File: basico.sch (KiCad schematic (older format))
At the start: 8 parts, among them P1 Power, P2 Analog, P3 Analog, P4 Digital, P5 PWM, P6 PWM, P7 Communication

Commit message: Clean up and add copper text
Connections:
- no-connect marks 63 -> 66
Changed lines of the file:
@@
 	7000 2050 7000 2150
 Wire Wire Line
-	7000 2050 7450 2050
+	7000 2050 7200 2050
 NoConn ~ 9350 1350
 Text Label 9250 1200 1    60   ~ 0
@@
 NoConn ~ 10000 4650
 NoConn ~ 10100 5650
-NoConn ~ 10300 4650
 NoConn ~ 10300 5650
 NoConn ~ 10400 5650
@@
 NoConn ~ 10400 1550
 NoConn ~ 10400 1650
-NoConn ~ 10400 1750
-NoConn ~ 10400 2750
 NoConn ~ 10400 2650
 NoConn ~ 10400 2550
@@
 Text Notes 1375 675  0    60   ~ 0
 Poncho Smart RAMPS para EDU-CIAA-NXP\n
+NoConn ~ 10400 3050
+NoConn ~ 10400 3150
+NoConn ~ 10400 1150
+NoConn ~ 10400 1250
+NoConn ~ 10200 5650
+NoConn ~ 9250 1200
+$Comp
+L basico-rescue:PWR_FLAG #FLG0101
+U 1 1 5D0FAD0D
+P 7200 2050
+F 0 "#FLG0101" H 7200 2145 30  0001 C CNN
+F 1 "PWR_FLAG" H 7200 2230 30  0000 C CNN
+F 2 "" H 7200 2050 60  0000 C CNN
+F 3 "" H 7200 2050 60  0000 C CNN
+	1    7200 2050
+	-1   0    0    1
+$EndComp
+Connection ~ 7200 2050
+Wire Wire Line
+	7200 2050 7450 2050
 $EndSCHEMATC

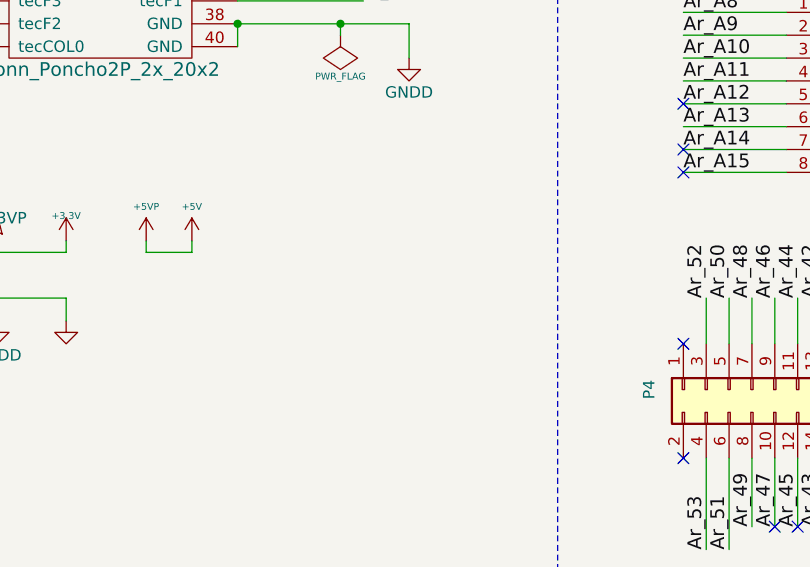
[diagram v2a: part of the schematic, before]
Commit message: Agregar led y re-ruteo
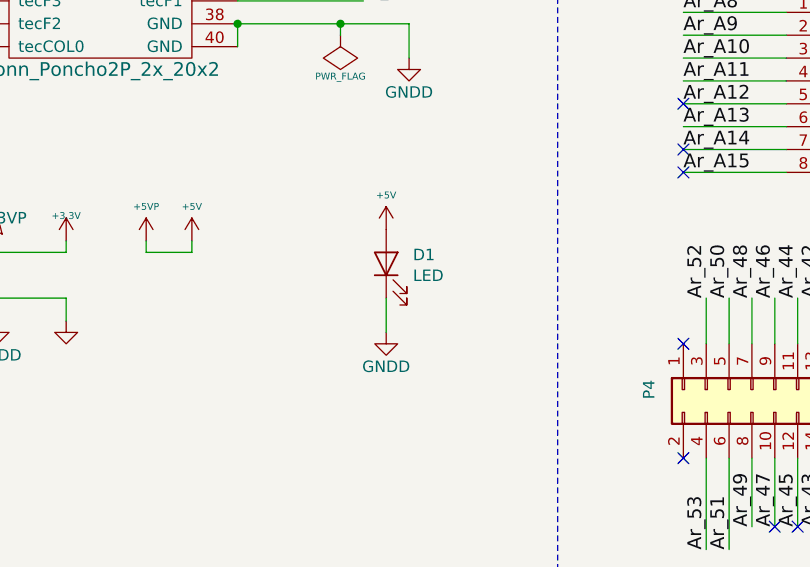
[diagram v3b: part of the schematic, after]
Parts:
- added D1: LED, LED_THT:LED_D3.0mm, symbol Device:LED
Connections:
- net +5V: now also D1.2 (A)
- net GND: now also D1.1 (K)
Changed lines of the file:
@@
 Sheet 1 1
 Title "Poncho Smart RAMPS para EDU-CIAA-NXP"
-Date "2019-06-17"
+Date "2019-06-24"
 Rev "1.0"
 Comp "Proyecto CIAA - COMPUTADORA INDUSTRIAL ABIERTA ARGENTINA"
-Comment1 "https://github.com/ciaa/Ponchos/tree/master/Basico/doc"
+Comment1 "https://github.com/dc740/smart-ramps-to-edu-ciaa"
 Comment2 "Licencia GPL v3 (Emilio Moretti - UNNOBA)"
 Comment3 "Ing. Moretti Emilio"
-Comment4 ""
+Comment4 "Revisor: Nelson Fortunatti"
 $EndDescr
 $Comp
@@
 Wire Wire Line
 	7200 2050 7450 2050
+$Comp
+L Device:LED D1
+U 1 1 5D12DF66
+P 7600 4500
+F 0 "D1" V 7639 4383 50  0000 R CNN
+F 1 "LED" V 7548 4383 50  0000 R CNN
+F 2 "LED_THT:LED_D3.0mm" H 7600 4500 50  0001 C CNN
+F 3 "~" H 7600 4500 50  0001 C CNN
+	1    7600 4500
+	0    -1   -1   0
+$EndComp
+$Comp
+L basico-rescue:+5V #PWR0103
+U 1 1 5D14A06A
+P 7600 4350
+F 0 "#PWR0103" H 7600 4440 20  0001 C CNN
+F 1 "+5V" H 7600 4500 30  0000 C CNN
+F 2 "" H 7600 4350 60  0000 C CNN
+F 3 "" H 7600 4350 60  0000 C CNN
+	1    7600 4350
+	1    0    0    -1
+$EndComp
+$Comp
+L basico-rescue:GNDD #PWR0104
+U 1 1 5D16F0C7
+P 7600 4800
+F 0 "#PWR0104" H 7600 4550 50  0001 C CNN
+F 1 "GNDD" H 7600 4650 50  0000 C CNN
+F 2 "" H 7600 4800 50  0000 C CNN
+F 3 "" H 7600 4800 50  0000 C CNN
+	1    7600 4800
+	1    0    0    -1
+$EndComp
+Wire Wire Line
+	7600 4650 7600 4800
 $EndSCHEMATC

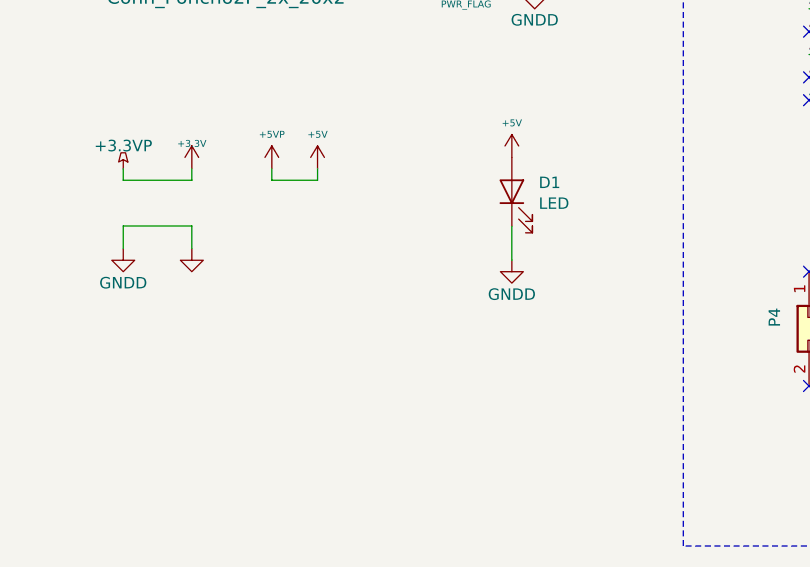
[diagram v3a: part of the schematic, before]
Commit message: Connect analog ground
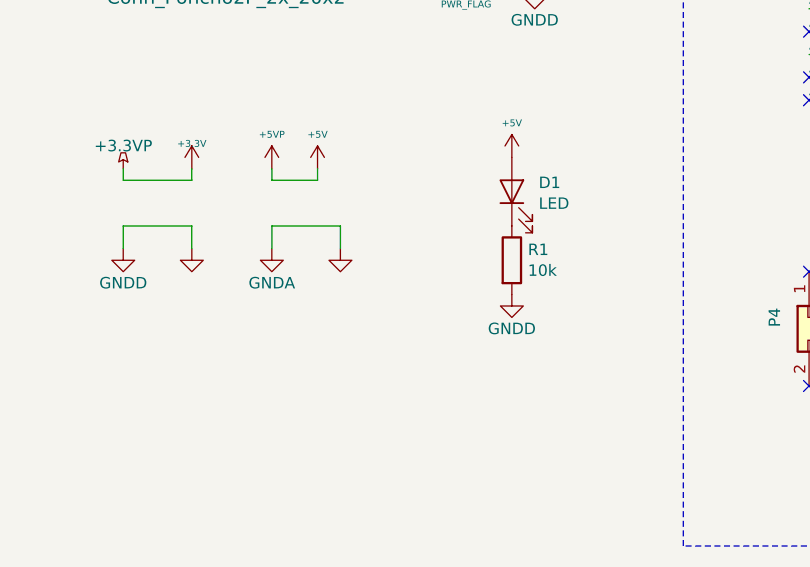
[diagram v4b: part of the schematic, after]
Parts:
- added R1: 10k, Resistor_THT:R_Axial_DIN0204_L3.6mm_D1.6mm_P5.08mm_Horizontal, symbol Device:R
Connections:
- net GNDA is gone; now on net GND: XA101.10 (GNDA), XA101.12 (GNDA), XA101.14 (GNDA), XA101.16 (GNDA), XA101.18 (GNDA), XA101.7 (GNDA), XA101.8 (GNDA)
- net GND: now also R1.2; no longer D1.1 (K)
- new net: D1.1 (K), R1.1
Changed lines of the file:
@@
 L basico-rescue:GNDD #PWR0104
 U 1 1 5D16F0C7
+P 7600 4950
+F 0 "#PWR0104" H 7600 4700 50  0001 C CNN
+F 1 "GNDD" H 7600 4800 50  0000 C CNN
+F 2 "" H 7600 4950 50  0000 C CNN
+F 3 "" H 7600 4950 50  0000 C CNN
+	1    7600 4950
+	1    0    0    -1
+$EndComp
+$Comp
+L Device:R R1
+U 1 1 5D13D3F8
 P 7600 4800
-F 0 "#PWR0104" H 7600 4550 50  0001 C CNN
-F 1 "GNDD" H 7600 4650 50  0000 C CNN
-F 2 "" H 7600 4800 50  0000 C CNN
-F 3 "" H 7600 4800 50  0000 C CNN
+F 0 "R1" H 7670 4846 50  0000 L CNN
+F 1 "10k" H 7670 4755 50  0000 L CNN
+F 2 "Resistor_THT:R_Axial_DIN0204_L3.6mm_D1.6mm_P5.08mm_Horizontal" V 7530 4800 50  0001 C CNN
+F 3 "~" H 7600 4800 50  0001 C CNN
 	1    7600 4800
 	1    0    0    -1
 $EndComp
+$Comp
+L basico-rescue:GND #PWR?
+U 1 1 5D15CEE1
+P 6850 4750
+F 0 "#PWR?" H 6850 4750 30  0001 C CNN
+F 1 "GND" H 6850 4680 30  0001 C CNN
+F 2 "" H 6850 4750 60  0000 C CNN
+F 3 "" H 6850 4750 60  0000 C CNN
+	1    6850 4750
+	1    0    0    -1
+$EndComp
 Wire Wire Line
-	7600 4650 7600 4800
+	6850 4650 6850 4750
+Wire Wire Line
+	6550 4650 6850 4650
+$Comp
+L basico-rescue:GNDA #PWR?
+U 1 1 5D166026
+P 6550 4750
+F 0 "#PWR?" H 6550 4500 50  0001 C CNN
+F 1 "GNDA" H 6550 4600 50  0000 C CNN
+F 2 "" H 6550 4750 50  0000 C CNN
+F 3 "" H 6550 4750 50  0000 C CNN
+	1    6550 4750
+	1    0    0    -1
+$EndComp
+Wire Wire Line
+	6550 4750 6550 4650
 $EndSCHEMATC
